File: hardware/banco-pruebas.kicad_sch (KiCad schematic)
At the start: 10 parts, among them P1 Clavija 5-15P, cable SJT 3×14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, Q1 Breaker 1P 15 A curva C (riel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, X0 Toma auxiliar (sin medir): me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, X1 Salida CH1 (15 A), X2 Salida CH2 (15 A)

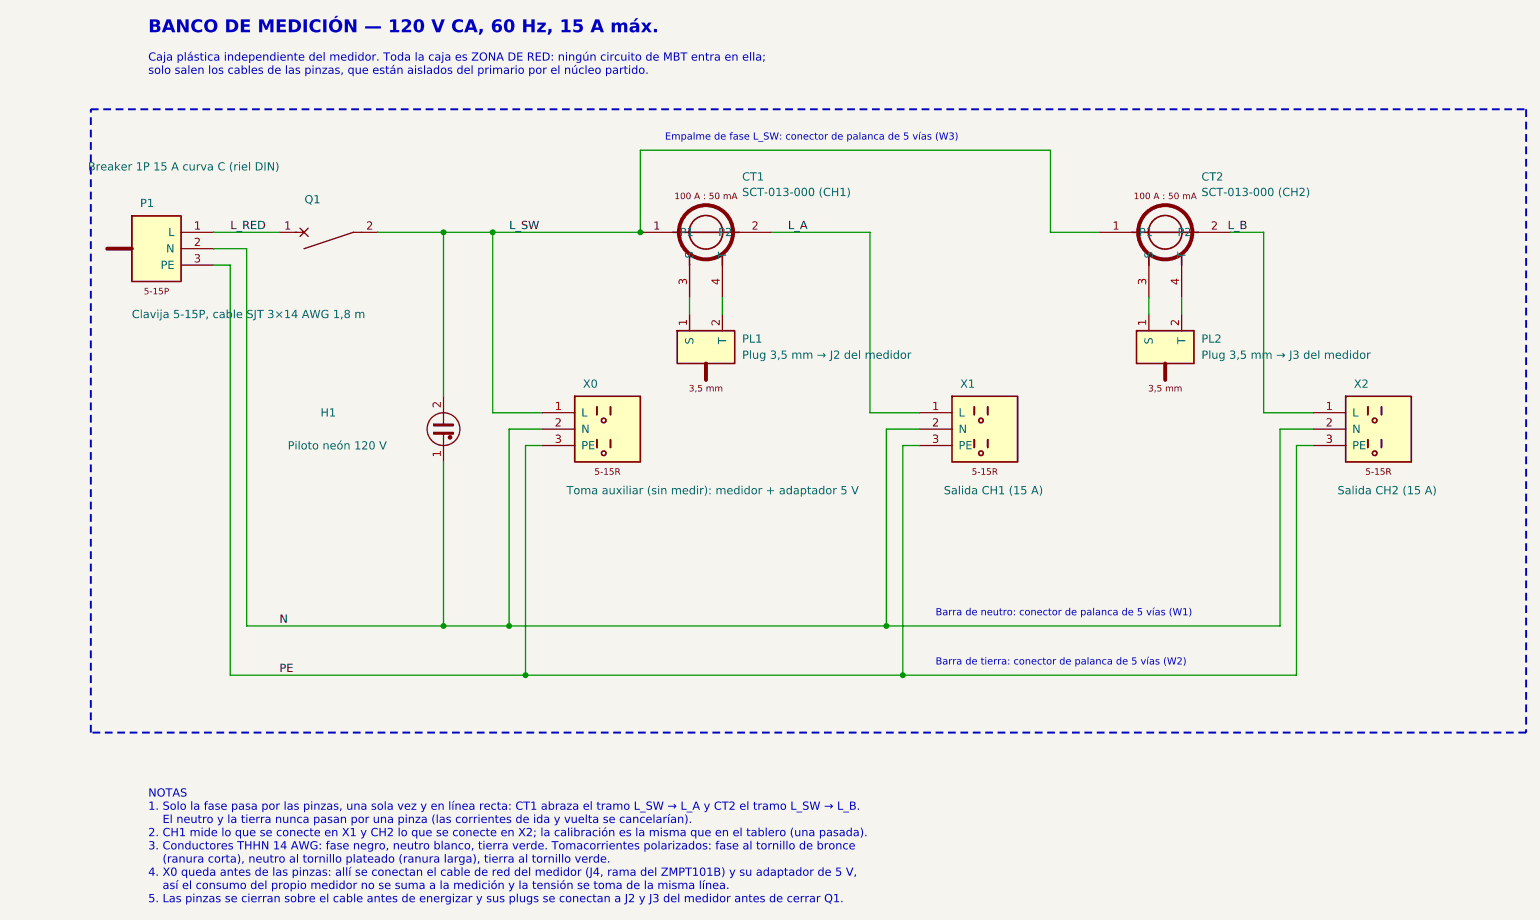
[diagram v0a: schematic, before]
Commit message: Simplificar el banco de medición: clavija, lazo de fase para la pinza y un tomacorriente
El banco queda en lo mínimo: se enchufa a la pared, la fase sale de la caja en un lazo
aislado donde se cierra la pinza y el equipo se conecta en un tomacorriente doble.
Se eliminan el breaker, el piloto, la toma auxiliar, la segunda pinza y los conectores.
Actualizados el esquemático de KiCad, el dibujo, el modelo de FreeCAD, las vistas y el
documento. Corrige también las referencias plurales a ilustraciones que quedaron sin numerar.
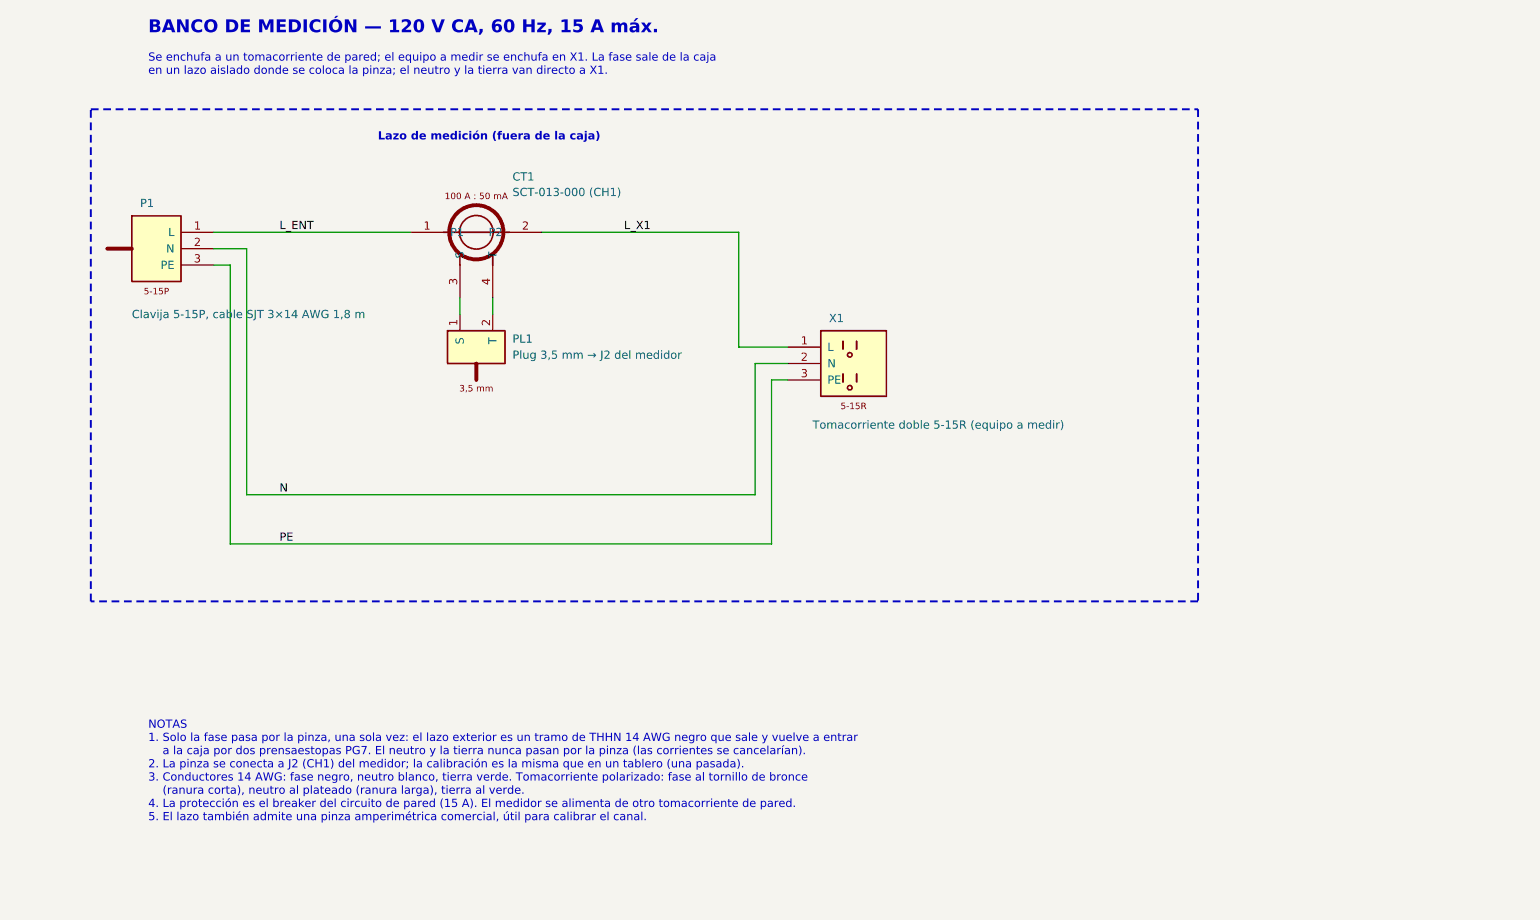
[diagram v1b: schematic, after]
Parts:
- removed CT1: SCT-013-000 (CH1), symbol Medidor:Pinza_SCT-013-000
- removed CT2: SCT-013-000 (CH2), symbol Medidor:Pinza_SCT-013-000
- removed PL1: Plug 3,5 mm → J2 del medidor, symbol Medidor:Plug_3.5mm
- removed PL2: Plug 3,5 mm → J3 del medidor, symbol Medidor:Plug_3.5mm
- removed X1: Salida CH1 (15 A), symbol Medidor:Tomacorriente_NEMA_5-15R
- removed X2: Salida CH2 (15 A), symbol Medidor:Tomacorriente_NEMA_5-15R
- CT1: renamed from Q1; value Breaker 1P 15 A curva C (riel DIN) -> SCT-013-000 (CH1); symbol Device:CircuitBreaker_1P -> Medidor:Pinza_SCT-013-000
- PL1: renamed from H1; value Piloto neón 120 V -> Plug 3,5 mm → J2 del medidor; symbol Device:Lamp_Neon -> Medidor:Plug_3.5mm
- X1: renamed from X0; value Toma auxiliar (sin medir): medidor + adaptador 5 V -> Tomacorriente doble 5-15R (equipo a medir)
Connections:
- net N: no longer PL1.1
- net L_RED renamed L_ENT
- net L_SW renamed L_X1
- net L_X1: no longer PL1.2
- new net: CT1.3 (S), PL1.1 (S)
- new net: CT1.4 (T), PL1.2 (T)
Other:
- note added: "Lazo de medición (fuera de la caja)"
- note added: "NOTAS 1. Solo la fase pasa por la pinza, una sola vez: el lazo exterior es un tramo de THHN 14 AWG negro que sale y vuelve a entrar a la caja por dos prensaestopas PG7. El neutro y la tierra nunca pasan por la pinza (las corrientes se cancelarían). 2. La pinza se conecta a J2 (CH1) del medidor; la calibración es la misma que en un tablero (una pasada). 3. Conductores 14 AWG: fase negro, neutro bl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"
- note added: "Se enchufa a un tomacorriente de pared; el equipo a medir se enchufa en X1. La fase sale de la caja en un lazo aislado donde se coloca la pinza; el neutro y la tierra van directo a X1."
- note removed: "Barra de neutro: conector de palanca de 5 vías (W1)"
- note removed: "Barra de tierra: conector de palanca de 5 vías (W2)"
- note removed: "Caja plástica independiente del medidor. Toda la caja es ZONA DE RED: ningún circuito de MBT entra en ella; solo salen los cables de las pinzas, que están aislados del primario por el núcleo partido."
- note removed: "Empalme de fase L_SW: conector de palanca de 5 vías (W3)"
- note removed: "NOTAS 1. Solo la fase pasa por las pinzas, una sola vez y en línea recta: CT1 abraza el tramo L_SW → L_A y CT2 el tramo L_SW → L_B. El neutro y la tierra nunca pasan por una pinza (las corrientes de ida y vuelta se cancelarían). 2. CH1 mide lo que se conecte en X1 y CH2 lo que se conecte en X2; la calibración es la misma que en el tablero (una pasada). 3. Conductores THHN 14 AWG: fase negro, neut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"
- moved on the sheet: X1

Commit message: Plataforma sobre Supabase, esquemáticos sin datos personales y redacción revisada
- plataforma: Postgres en Supabase con postgres.js (DATABASE_URL) en lugar de SQLite;
  migración en supabase/migrations con RLS activo; ingesta por lotes en una transacción;
  pnpm db:migrar y .env.ejemplo; pruebas del servicio contra un Postgres de pruebas
- Esquemáticos, PCB y figuras sin nombres ni referencias a asignaturas (revisión B)
- Redacción del documento revisada para un tono más directo y sin exagerar el avance
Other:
- company: Universidad de la Costa (CUC) — Sistemas Embebidos 1 -> (none)
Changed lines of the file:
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@@
 	(title_block
 		(title "Banco de medición con tomacorriente de entrada y salida")
-		(date "2026-10-16")
-		(rev "C2-A")
-		(company "Universidad de la Costa (CUC) — Sistemas Embebidos 1")
-		(comment 1 "David Orozco · Jose Torres · Leo Rojas")
+		(date "2026-10-21")
+		(rev "B")
+		(company "")
+		(comment 1 "")
 		(comment 2 "Complemento del medidor de energía de dos canales")
 	)
